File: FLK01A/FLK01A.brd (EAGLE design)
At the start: 30.5 x 30.5 mm, 30 parts, among them J1 M10SMD_MALE, J2 M10SMD_MALE, U1 LPC812TSSOP20, U2 EKMBTO5, U3 HTU21DSMD, U4 MMA8452Q, U5 VCNL4000, U6 MPL3115A2LGA8, Y1 12MHZ

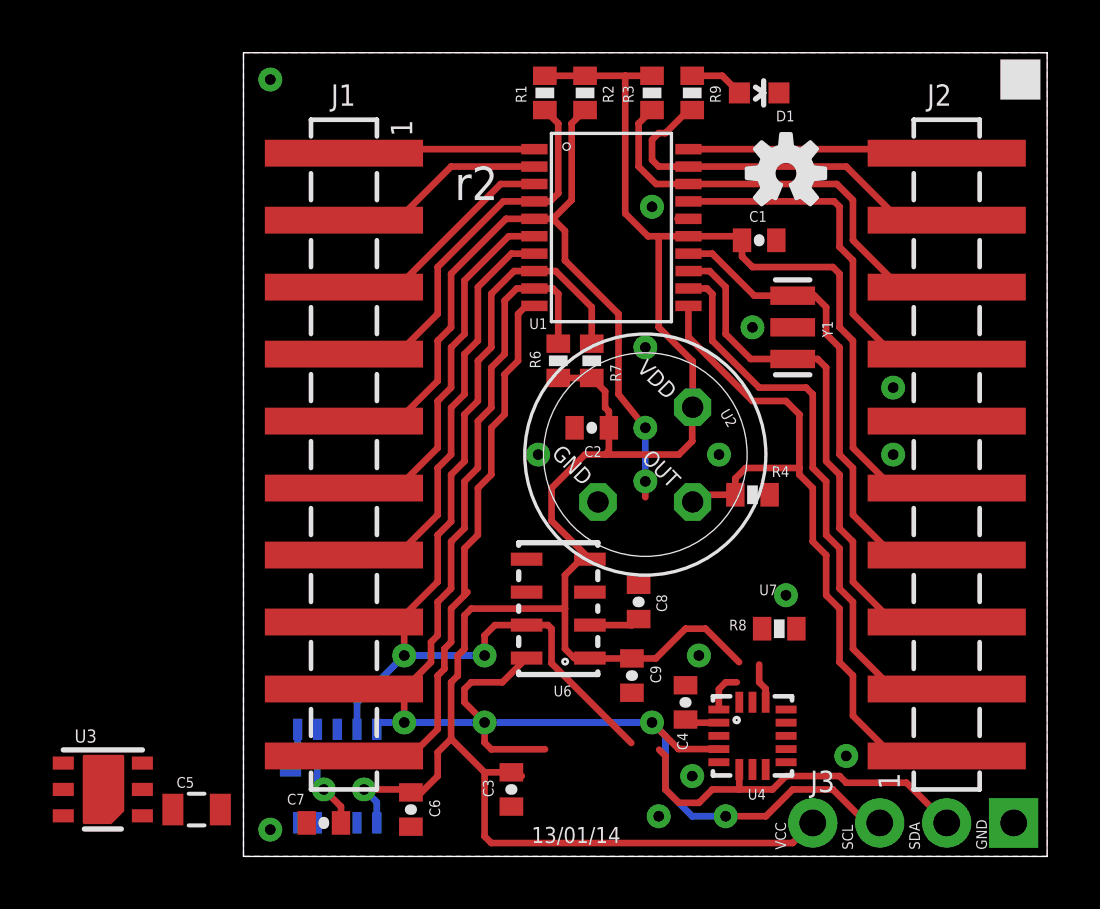
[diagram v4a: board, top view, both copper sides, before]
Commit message: [pcb] rename passives
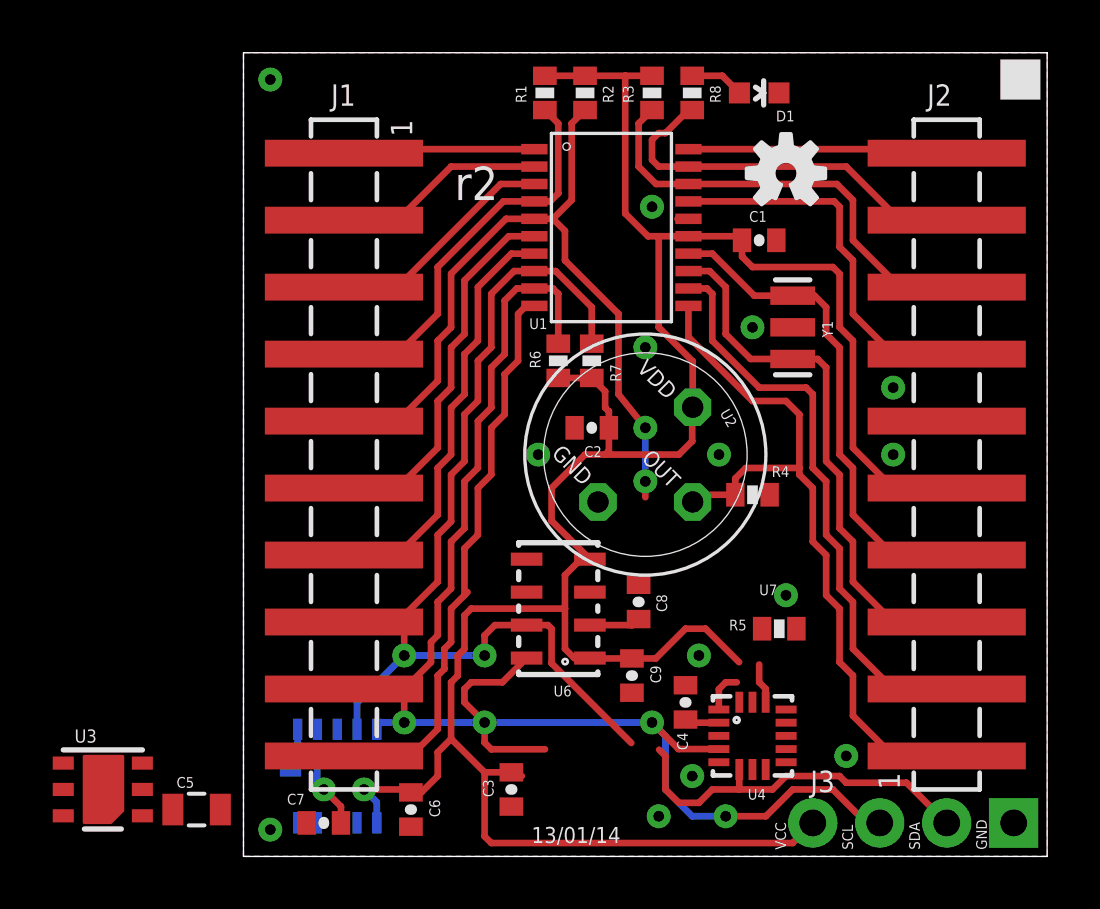
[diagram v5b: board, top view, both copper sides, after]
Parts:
- removed R9: 1k, SparkFun-Passives:0402-RES
- added R5: 100k, SparkFun-Passives:0402-RES
- R8: value 100k -> 1k
- moved R8 20.6 mm to (17.0, 29.0), turned to 270 degrees
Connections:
- net GND: now also R5.1; no longer R8.1
- net ISP_RXD: now also R8.2; no longer R9.2
- net MMA_INT: now also R5.2; no longer R8.2
- net N$8: now also R8.1; no longer R9.1
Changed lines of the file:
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@@
 <attribute name="NAME" x="16.4465" y="4.699" size="0.4064" layer="25" rot="R270"/>
 </element>
-<element name="R8" library="SparkFun-Passives" package="0402-RES" value="100k" x="20.32" y="8.636" smashed="yes">
+<element name="R5" library="SparkFun-Passives" package="0402-RES" value="100k" x="20.32" y="8.636" smashed="yes">
 <attribute name="NAME" x="18.415" y="8.5725" size="0.4064" layer="25"/>
 </element>
@@
 <attribute name="NAME" x="20.193" y="27.8765" size="0.4064" layer="25"/>
 </element>
-<element name="R9" library="SparkFun-Passives" package="0402-RES" value="1k" x="17.018" y="28.956" smashed="yes" rot="R270">
+<element name="R8" library="SparkFun-Passives" package="0402-RES" value="1k" x="17.018" y="28.956" smashed="yes" rot="R270">
 <attribute name="NAME" x="18.0975" y="28.575" size="0.4064" layer="25" rot="R90"/>
 </element>
@@
 <via x="17.018" y="3.048" extent="1-16" drill="0.4064" diameter="0.6096"/>
 <contactref element="R4" pad="1"/>
-<contactref element="R8" pad="1"/>
+<contactref element="R5" pad="1"/>
 <contactref element="C5" pad="2"/>
 <contactref element="U3" pad="GND"/>
@@
 <wire x1="6.35" y1="3.81" x2="3.81" y2="3.81" width="0.254" layer="1"/>
 <contactref element="U4" pad="11"/>
-<contactref element="R8" pad="2"/>
+<contactref element="R5" pad="2"/>
 <wire x1="20.579" y1="4.572" x2="20.97" y2="8.636" width="0" layer="19" extent="1-1"/>
 <wire x1="8.499" y1="10.023" x2="20.97" y2="8.636" width="0" layer="19" extent="1-1"/>
@@
 <wire x1="22.8596" y1="26.1624" x2="24.892" y2="24.13" width="0.254" layer="1"/>
 <wire x1="24.892" y1="24.13" x2="26.67" y2="24.13" width="0.254" layer="1"/>
-<contactref element="R9" pad="2"/>
+<contactref element="R8" pad="2"/>
 <wire x1="16.875" y1="26.1624" x2="15.7476" y2="26.1624" width="0.254" layer="1"/>
 <wire x1="15.7476" y1="26.1624" x2="15.494" y2="26.416" width="0.254" layer="1"/>
@@
 </signal>
 <signal name="N$8">
-<contactref element="R9" pad="1"/>
+<contactref element="R8" pad="1"/>
 <contactref element="D1" pad="A"/>
 <wire x1="17.018" y1="29.606" x2="18.158" y2="29.606" width="0.254" layer="1"/>

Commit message: [pcb] update board layout
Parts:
- U3: device SparkFun-Sensors:HTU21D -> flukso:HTU21D
- moved C5 23.0 mm to (20.3, 8.13)
- moved U3 16.5 mm to (11.2, 2.79), turned to 180 degrees
- moved C3 4.10 mm to (14.2, 2.03)
- moved R5 2.81 mm to (20.6, 11.4), turned to 270 degrees
- moved C2 1.27 mm to (14.5, 16.3), turned to 270 degrees
- moved C4 1.05 mm to (17.0, 6.86)
- moved U4 0.72 mm to (19.8, 5.08)
- moved C9 0.51 mm to (15.2, 6.86)
- moved C8 0.36 mm to (15.2, 9.40)
- moved R4 0.25 mm to (19.3, 14.0)
- moved U6 0.25 mm to (12.2, 9.40)
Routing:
- net MMA_INT: track 21.9 -> 43.0 mm, vias 0 -> 2
- net ISP_TXD: track 29.8 -> 17.8 mm, vias 2 -> 0
- net 3.3V: track 100.7 -> 106.6 mm
- net I2C0_SDA: track 53.5 -> 59.0 mm
- net I2C0_SCL: track 57.6 -> 52.8 mm
- net GND: track 0.42 -> 1.58 mm, vias 15 -> 17
- net N$3: track 1.31 -> 1.95 mm
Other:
- board text added: "15/11/14"
- board text removed: "13/01/14"
- board text removed: "U7"

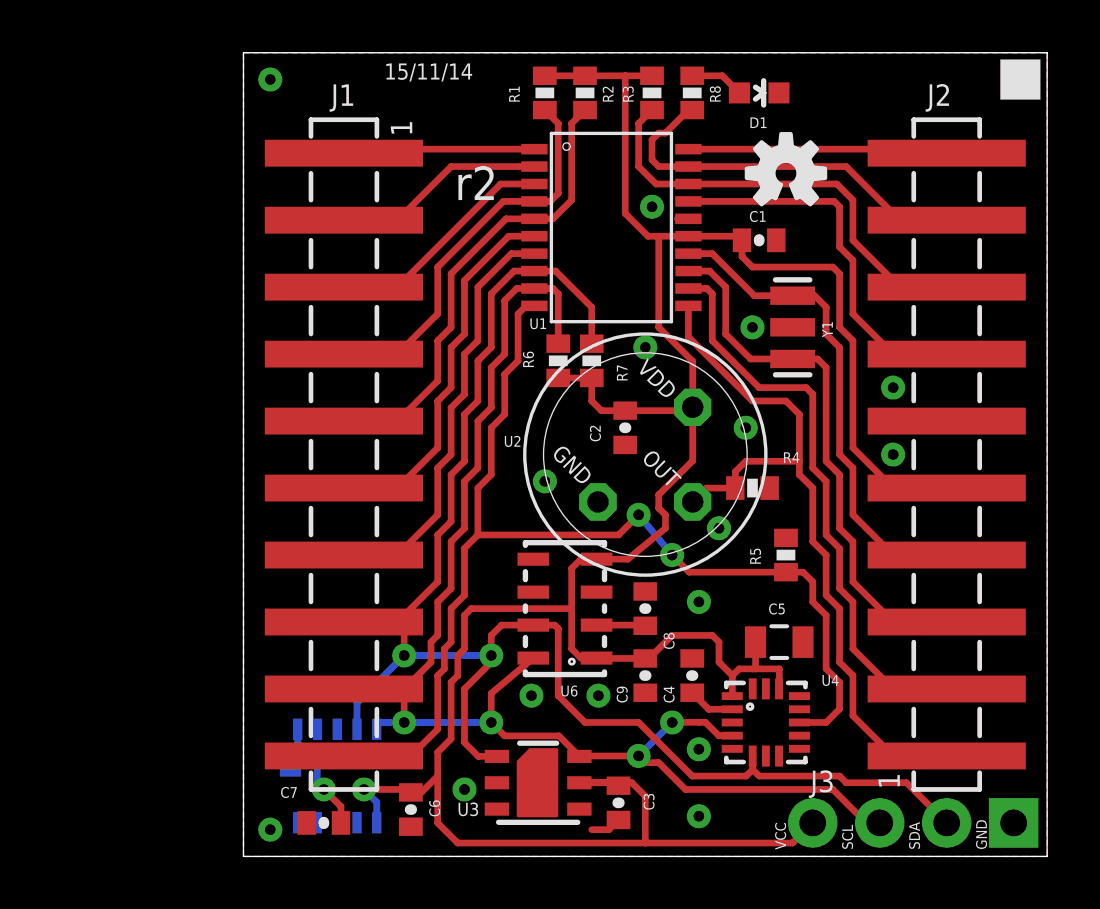
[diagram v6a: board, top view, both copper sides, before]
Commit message: [pcb] use smaller + round pads for I2C header
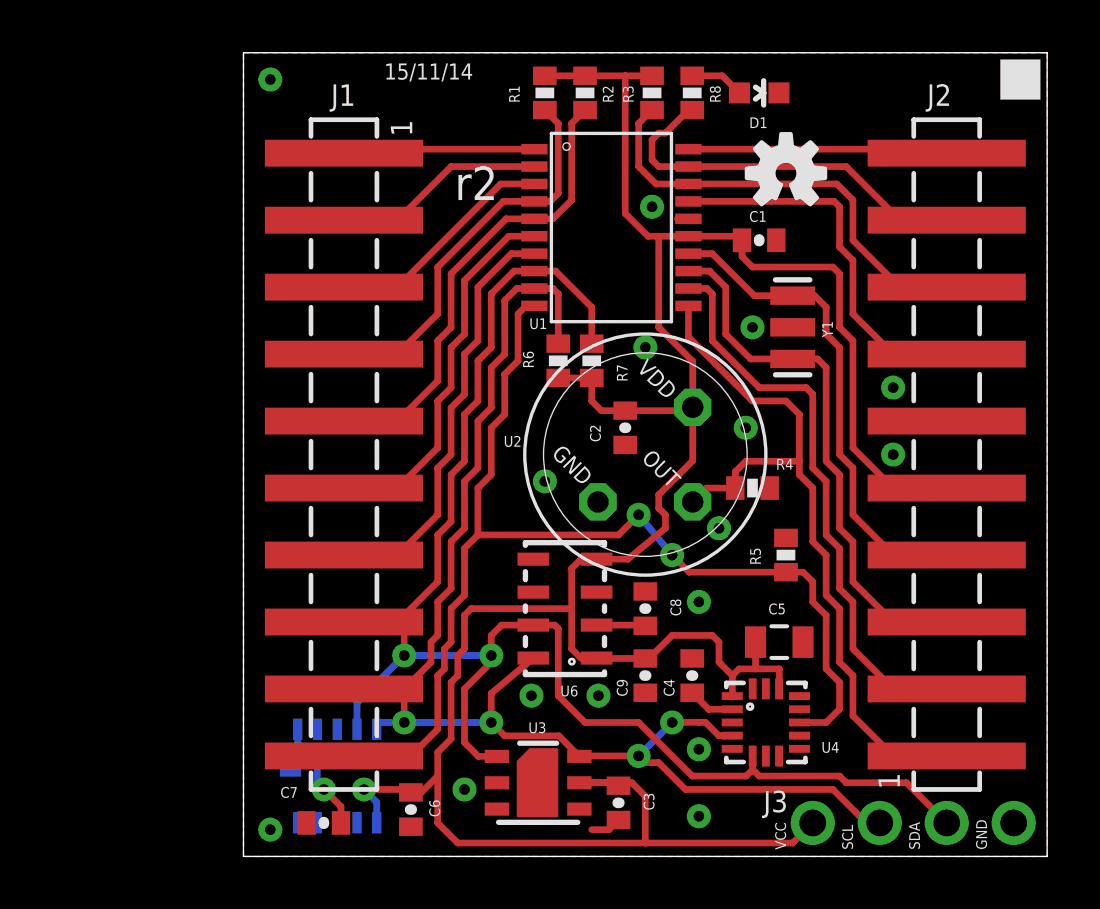
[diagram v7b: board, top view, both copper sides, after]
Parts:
- J3: device SparkFun-Connectors:1X04_NO_SILK -> flukso:1X04_NO_SILK
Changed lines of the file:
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@@
 <grid distance="0.01" unitdist="inch" unit="inch" style="lines" multiple="1" display="yes" altdistance="0.005" altunitdist="inch" altunit="inch"/>
 <layers>
-<layer number="1" name="Top" color="4" fill="1" visible="yes" active="yes"/>
-<layer number="16" name="Bottom" color="1" fill="1" visible="yes" active="yes"/>
+<layer number="1" name="Top" color="4" fill="1" visible="no" active="yes"/>
+<layer number="16" name="Bottom" color="1" fill="1" visible="no" active="yes"/>
 <layer number="17" name="Pads" color="2" fill="1" visible="yes" active="yes"/>
 <layer number="18" name="Vias" color="2" fill="1" visible="yes" active="yes"/>
@@
 <layer number="54" name="bGND_GNDA" color="1" fill="9" visible="no" active="no"/>
 <layer number="56" name="wert" color="7" fill="1" visible="no" active="yes"/>
+<layer number="57" name="tCAD" color="7" fill="1" visible="no" active="no"/>
 <layer number="91" name="Nets" color="2" fill="1" visible="no" active="no"/>
 <layer number="92" name="Busses" color="1" fill="1" visible="no" active="no"/>
@@
 <layer number="97" name="Info" color="7" fill="1" visible="no" active="no"/>
 <layer number="98" name="Guide" color="6" fill="1" visible="no" active="no"/>
+<layer number="99" name="SpiceOrder" color="7" fill="1" visible="no" active="no"/>
 <layer number="100" name="Muster" color="7" fill="1" visible="no" active="no"/>
 <layer number="101" name="Patch_Top" color="12" fill="4" visible="no" active="yes"/>
@@
 <layer number="132" name="test" color="7" fill="1" visible="yes" active="yes"/>
 <layer number="144" name="Drill_legend" color="7" fill="1" visible="no" active="yes"/>
+<layer number="150" name="Notes" color="7" fill="1" visible="yes" active="yes"/>
 <layer number="151" name="HeatSink" color="7" fill="1" visible="no" active="yes"/>
 <layer number="152" name="_bDocu" color="7" fill="1" visible="yes" active="yes"/>
+<layer number="153" name="FabDoc1" color="7" fill="1" visible="yes" active="yes"/>
+<layer number="154" name="FabDoc2" color="7" fill="1" visible="yes" active="yes"/>
+<layer number="155" name="FabDoc3" color="7" fill="1" visible="yes" active="yes"/>
 <layer number="199" name="Contour" color="7" fill="1" visible="yes" active="yes"/>
 <layer number="200" name="200bmp" color="1" fill="10" visible="no" active="no"/>
@@
 </element>
 <element name="R4" library="SparkFun-Passives" package="0402-RES" value="100k" x="19.304" y="13.97" smashed="yes" rot="R180">
-<attribute name="NAME" x="20.447" y="14.9225" size="0.4064" layer="25"/>
+<attribute name="NAME" x="20.193" y="14.6685" size="0.4064" layer="25"/>
 </element>
 <element name="C3" library="flukso" package="0402-CAP" value="100nF" x="14.224" y="2.032" smashed="yes" rot="R270">
@@
 <element name="U4" library="SparkFun-Sensors" package="QFN-16_0.5MM" value="MMA8452Q" x="19.812" y="5.08" smashed="yes">
 <attribute name="PROD_ID" value="IC-10769" x="19.812" y="5.08" size="1.778" layer="27" display="off"/>
-<attribute name="NAME" x="21.918" y="6.472" size="0.4064" layer="25"/>
+<attribute name="NAME" x="21.918" y="3.932" size="0.4064" layer="25"/>
 </element>
 <element name="C4" library="flukso" package="0402-CAP" value="100nF" x="17.018" y="6.858" smashed="yes" rot="R90">
-<attribute name="NAME" x="15.9385" y="6.477" size="0.4064" layer="25" rot="R270"/>
+<attribute name="NAME" x="15.9385" y="6.731" size="0.4064" layer="25" rot="R270"/>
 </element>
 <element name="R5" library="SparkFun-Passives" package="0402-RES" value="100k" x="20.574" y="11.43" smashed="yes" rot="R270">
@@
 </element>
 <element name="C8" library="flukso" package="0402-CAP" value="100nF" x="15.24" y="9.398" smashed="yes" rot="R90">
-<attribute name="NAME" x="15.9385" y="8.509" size="0.4064" layer="25" rot="R270"/>
+<attribute name="NAME" x="16.1925" y="9.779" size="0.4064" layer="25" rot="R270"/>
 </element>
 <element name="C9" library="flukso" package="0402-CAP" value="100nF" x="15.24" y="6.858" smashed="yes" rot="R270">
-<attribute name="NAME" x="14.1605" y="6.477" size="0.4064" layer="25" rot="R270"/>
+<attribute name="NAME" x="14.1605" y="6.731" size="0.4064" layer="25" rot="R270"/>
 </element>
 <element name="D1" library="SparkFun-LED" package="LED-0603" value="GREEN" x="19.558" y="28.956" smashed="yes" rot="R270">
@@
 </element>
 <element name="U$2" library="flukso" package="FLUKSO_LOGO_MEDIUM" value="" x="22.098" y="24.638" rot="MR0"/>
-<element name="J3" library="SparkFun-Connectors" package="1X04_NO_SILK" value="" x="29.21" y="1.27" smashed="yes" rot="R180">
-<attribute name="NAME" x="22.4282" y="3.2512" size="0.8128" layer="25" font="vector" ratio="10" rot="R180"/>
-<attribute name="VALUE" x="30.48" y="4.445" size="1.27" layer="27" rot="R180"/>
-</element>
 <element name="C5" library="flukso" package="0805" value="4.7uF" x="20.32" y="8.128" smashed="yes">
 <attribute name="NAME" x="20.574" y="9.5885" size="0.4064" layer="25" rot="R180"/>
 </element>
 <element name="U3" library="flukso" package="HTU21D" value="HTU21DSMD" x="11.176" y="2.794" smashed="yes" rot="R180">
-<attribute name="NAME" x="8.949" y="2.035" size="0.5" layer="25" rot="R180"/>
+<attribute name="NAME" x="11.489" y="5.083" size="0.4064" layer="25" rot="R180"/>
+</element>
+<element name="J3" library="flukso" package="1X04_NO_SILK" value="" x="29.21" y="1.27" smashed="yes" rot="R180">
+<attribute name="NAME" x="20.6502" y="2.4892" size="0.8128" layer="25" font="vector" ratio="10" rot="R180"/>
+<attribute name="VALUE" x="30.48" y="4.445" size="1.27" layer="27" rot="R180"/>
 </element>
 </elements>
@@
 <via x="17.272" y="4.064" extent="1-16" drill="0.4064" diameter="0.6096"/>
 <contactref element="D1" pad="C"/>
-<contactref element="J3" pad="1"/>
 <via x="8.382" y="2.54" extent="1-16" drill="0.4064" diameter="0.6096"/>
 <contactref element="R4" pad="1"/>
@@
 <via x="17.272" y="1.524" extent="1-16" drill="0.4064" diameter="0.6096"/>
 <via x="17.272" y="9.652" extent="1-16" drill="0.4064" diameter="0.6096"/>
+<contactref element="J3" pad="1"/>
 </signal>
 <signal name="RFM_IRQ">
@@
 <wire x1="13.208" y1="20.828" x2="11.836" y2="22.2" width="0.254" layer="1"/>
 <wire x1="11.836" y1="22.2" x2="11.027" y2="22.2" width="0.254" layer="1"/>
-<contactref element="J3" pad="2"/>
-<wire x1="25.146" y1="2.794" x2="26.67" y2="1.27" width="0.254" layer="1"/>
 <wire x1="22.606" y1="3.048" x2="22.86" y2="2.794" width="0.254" layer="1"/>
 <wire x1="22.86" y1="2.794" x2="25.146" y2="2.794" width="0.254" layer="1"/>
@@
 <wire x1="8.382" y1="4.318" x2="8.906" y2="3.794" width="0.254" layer="1"/>
 <wire x1="8.906" y1="3.794" x2="9.6125" y2="3.794" width="0.254" layer="1"/>
+<contactref element="J3" pad="2"/>
+<wire x1="25.146" y1="2.794" x2="26.67" y2="1.27" width="0.254" layer="1"/>
 </signal>
 <signal name="I2C0_SCL">
@@
 <wire x1="7.112" y1="8.128" x2="7.112" y2="7.366" width="0.254" layer="1"/>
 <wire x1="7.112" y1="7.366" x2="5.969" y2="6.223" width="0.254" layer="1"/>
-<contactref element="J3" pad="3"/>
-<wire x1="24.13" y1="1.27" x2="23.622" y2="1.27" width="0.254" layer="1"/>
 <wire x1="23.622" y1="1.27" x2="22.352" y2="2.54" width="0.254" layer="1"/>
 <wire x1="22.352" y1="2.54" x2="16.764" y2="2.54" width="0.254" layer="1"/>
@@
 <wire x1="12.7555" y1="3.81" x2="14.986" y2="3.81" width="0.254" layer="1"/>
 <wire x1="11.9615" y1="4.572" x2="12.7395" y2="3.794" width="0.254" layer="1"/>
+<contactref element="J3" pad="3"/>
+<wire x1="23.622" y1="1.27" x2="24.13" y2="1.27" width="0.254" layer="1"/>
 </signal>
 <signal name="MMA_INT">
@@
 <wire x1="8.636" y1="9.398" x2="12.446" y2="9.398" width="0.254" layer="1"/>
 <wire x1="15.748" y1="20.066" x2="15.748" y2="23.5208" width="0.254" layer="1"/>
-<contactref element="J3" pad="4"/>
-<wire x1="21.59" y1="1.27" x2="20.828" y2="0.508" width="0.254" layer="1"/>
 <wire x1="20.828" y1="0.508" x2="15.24" y2="0.508" width="0.254" layer="1"/>
 <wire x1="15.24" y1="0.508" x2="8.128" y2="0.508" width="0.254" layer="1"/>
@@
 <wire x1="14.732" y1="2.794" x2="15.24" y2="2.286" width="0.254" layer="1"/>
 <wire x1="15.24" y1="2.286" x2="15.24" y2="0.508" width="0.254" layer="1"/>
-<wire x1="18.796" y1="7.112" x2="19.304" y2="7.112" width="0.254" layer="1"/>
+<wire x1="18.796" y1="7.112" x2="19.42" y2="7.112" width="0.254" layer="1"/>
 <wire x1="19.42" y1="7.112" x2="20.32" y2="7.112" width="0.254" layer="1"/>
 <wire x1="20.312" y1="6.355" x2="20.32" y2="6.363" width="0.254" layer="1"/>
 <wire x1="20.32" y1="6.363" x2="20.32" y2="7.112" width="0.254" layer="1"/>
 <wire x1="19.42" y1="8.128" x2="19.42" y2="7.112" width="0.254" layer="1"/>
-<wire x1="19.42" y1="7.112" x2="19.304" y2="7.112" width="0.254" layer="1"/>
+<contactref element="J3" pad="4"/>
+<wire x1="20.828" y1="0.508" x2="21.59" y2="1.27" width="0.254" layer="1"/>
 </signal>
 <signal name="QSPY_RXD">

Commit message: [flk/flr] introduce r3 of sensor and radio board
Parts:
- removed J3: (no value), flukso:1X04_NO_SILK
- added C10: 100nF, flukso:0402-CAP
- C5: device flukso:0805 -> flukso:C0805K
- J1, J2: value M10SMD_MALE -> M10SMD_MALE_SHORT; device flukso:1X10_SMD_MALE -> flukso:1X10_SMD_MALE_SHORT
- moved C5 11.3 mm to (10.9, 1.78), turned to 180 degrees
- moved R5 10.7 mm to (10.9, 16.0), turned to 180 degrees
- moved C3 9.01 mm to (10.9, 10.4), turned to 90 degrees
- moved U4 8.40 mm to (11.4, 4.57), turned to 180 degrees
- moved C8 8.19 mm to (22.4, 5.33)
- moved U6 7.61 mm to (19.1, 6.10)
- moved C9 7.26 mm to (21.1, 2.54), turned to 0 degrees
- moved U3 6.48 mm to (14.0, 8.64), turned to 0 degrees
- moved C4 3.88 mm to (15.0, 3.56), turned to 0 degrees
- moved R6 0.36 mm to (12.2, 19.1)
- moved R7 0.36 mm to (13.5, 19.1)
- moved C2 0.25 mm to (14.5, 16.0), turned to 180 degrees
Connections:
- removed net N$7: U6.3
- net 3.3V: no longer J3.4
- net EKMB_INT: now also C10.1
- net GND: now also C10.2, U6.3; no longer J3.1
- net I2C0_SCL: no longer J3.3
- net I2C0_SDA: no longer J3.2
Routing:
- net MMA_INT: track 43.0 -> 27.6 mm, vias 2 -> 0
- net I2C0_SDA: track 59.0 -> 43.6 mm
- net 3.3V: track 106.6 -> 95.5 mm
- net I2C0_SCL: track 52.8 -> 47.7 mm, vias 4 -> 3
- net EKMB_INT: track 29.7 -> 27.2 mm
- net QSPY_RXD: track 18.5 -> 21.0 mm
- net GND: track 1.58 -> 3.52 mm, vias 17 -> 14
- net RFM_SCK: track 14.3 -> 12.5 mm
- net ISP_TXD: track 17.8 -> 16.0 mm
- net SWDIO: track 16.1 -> 14.3 mm
- net SWCLK: track 14.3 -> 15.8 mm
- net RFM_SDO: track 8.06 -> 9.59 mm
- net RFM_IRQ: track 7.29 -> 5.76 mm
- net RFM_SEL: track 9.86 -> 11.4 mm
- net PIO0_6: track 16.8 -> 18.3 mm
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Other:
- board text added: "17/02/15"
- board text added: "r3"
- board text removed: "15/11/14"
- board text removed: "GND"
- board text removed: "SCL"
- board text removed: "SDA"
- board text removed: "VCC"
- board text removed: "r2"
